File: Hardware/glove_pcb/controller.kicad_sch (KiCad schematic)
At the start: 10 parts, among them J6 ISCP, J7 Debug Serial, U2 MCP3008, U4 ATmega328PB-A

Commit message: Finish controller pin assignments
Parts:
- added C18, C20: 10uF, symbol Device:C
- added C19, C21: 0.1uF, symbol Device:C
- added J19: Bluetooth, symbol Connector_Generic:Conn_01x06
- added R7: 1k, symbol Device:R
- added R8: 2k, symbol Device:R
- added U6, U7: MCP3008, symbol Analog_ADC:MCP3008
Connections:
- net GND: now also C18.2, C19.2, C20.2, C21.2, J19.4 (Pin_4), R8.2, U6.14 (AGND), U6.9 (DGND), U7.14 (AGND), U7.9 (DGND)
- net MISO1: now also U6.12 (Dout), U7.12 (Dout)
- net MOSI1: now also U6.11 (Din), U7.11 (Din)
- net SCK1: now also U6.13 (CLK), U7.13 (CLK)
- net SS_ADC2: now also U6.10 (~{CS}/SHDN)
- net SS_ADC3: now also U7.10 (~{CS}/SHDN)
- net VCC_UC: now also C18.1, C19.1, C20.1, C21.1, U6.15 (Vref), U6.16 (Vdd), U7.15 (Vref), U7.16 (Vdd)
- net OC2B: now reaches U4.1 (PD3)
- net OC0A: now reaches U4.10 (PD6)
- net UC_MOTOR_PMODE: now reaches U4.11 (PD7)
- net UC_MOTOR_SLEEP: now reaches U4.12 (PB0)
- net OC1A: now reaches U4.13 (PB1)
- net OC1B: now reaches U4.14 (PB2)
- net MOTOR5_FAULT: now reaches U4.2 (PD4)
- net UC_MOTOR_PH2: now reaches U4.27 (PC4)
- net UC_MOTOR_PH3: now reaches U4.28 (PC5)
- net MOTOR3_FAULT: now reaches U4.3 (PE0)
- net RXD: now reaches U4.30 (PD0)
- net RXD: now also J19.3 (Pin_3)
- net TXD: now reaches U4.31 (PD1)
- net TXD: now also R7.1
- net UC_MOTOR_PH1: now reaches U4.32 (PD2)
- net MOTOR4_FAULT: now reaches U4.6 (PE1)
- net MOTOR1_FAULT: now reaches U4.7 (XTAL1/PB6)
- net MOTOR2_FAULT: now reaches U4.8 (XTAL2/PB7)
- net OC0B: now reaches U4.9 (PD5)
- new net: J19.2 (Pin_2), R7.2, R8.1
- new net VCC_BT: J19.5 (Pin_5)
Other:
- moved on the sheet: C12, C13, R6, U2

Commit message: Minor changes from meeting with dmitry
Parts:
- removed C8: 0.1uF, symbol Device:C
- removed J19: Bluetooth, symbol Connector_Generic:Conn_01x06
- removed R7: 1k, symbol Device:R
- removed R8: 2k, symbol Device:R
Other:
- moved on the sheet: C20, C21, R6, U7

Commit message: Yet more improvements to the schematic
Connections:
- net DBG_RX is gone; now on net MISO: J7.2 (Pin_2)
- net DBG_TX is gone; now on net MOSI: J7.3 (Pin_3)
- net GND: no longer J7.5 (Pin_5)
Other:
- moved on the sheet: C12, C13, C18, C19, C20, C21, U2, U6, U7

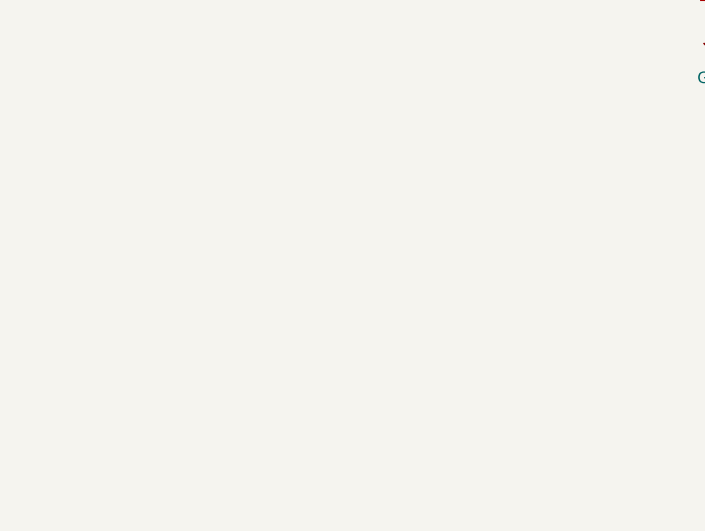
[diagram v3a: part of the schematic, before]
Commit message: Add logic level shifter to controller schematic
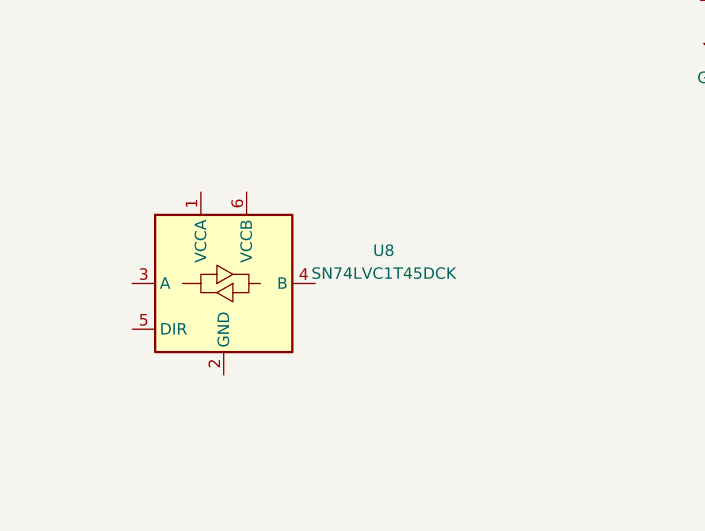
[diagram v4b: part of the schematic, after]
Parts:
- added U8: SN74LVC1T45DCK, Package_TO_SOT_SMD:SOT-363_SC-70-6, symbol Logic_LevelTranslator:SN74LVC1T45DCK
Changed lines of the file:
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@@
+    )
+  )
+  (symbol (lib_id "Logic_LevelTranslator:SN74LVC1T45DCK") (at 40.64 138.43 0) (unit 1)
+    (in_bom yes) (on_board yes) (dnp no) (fields_autoplaced)
+    (property "Reference" "U8" (at 58.42 134.7821 0)
+      (effects (font (size 1.27 1.27)))
+    )
+    (property "Value" "SN74LVC1T45DCK" (at 58.42 137.3221 0)
+      (effects (font (size 1.27 1.27)))
+    )
+    (property "Footprint" "Package_TO_SOT_SMD:SOT-363_SC-70-6" (at 40.64 149.86 0)
+      (effects (font (size 1.27 1.27)) hide)
+    )
+    (property "Datasheet" "http://www.ti.com/lit/ds/symlink/sn74lvc1t45.pdf" (at 17.78 154.94 0)
+      (effects (font (size 1.27 1.27)) hide)
+    )
+    (pin "1")
+    (pin "5")
+    (pin "4")
+    (pin "2")
+    (pin "6")
+    (pin "3")
+    (instances
+      (project "glove_pcb"
+        (path "/747ff5f3-d342-40b0-8e4e-75b3a3063e75/ecec443b-784e-4f7b-9f78-072e3afadba0"
+          (reference "U8") (unit 1)
+        )
+      )
     )
   )

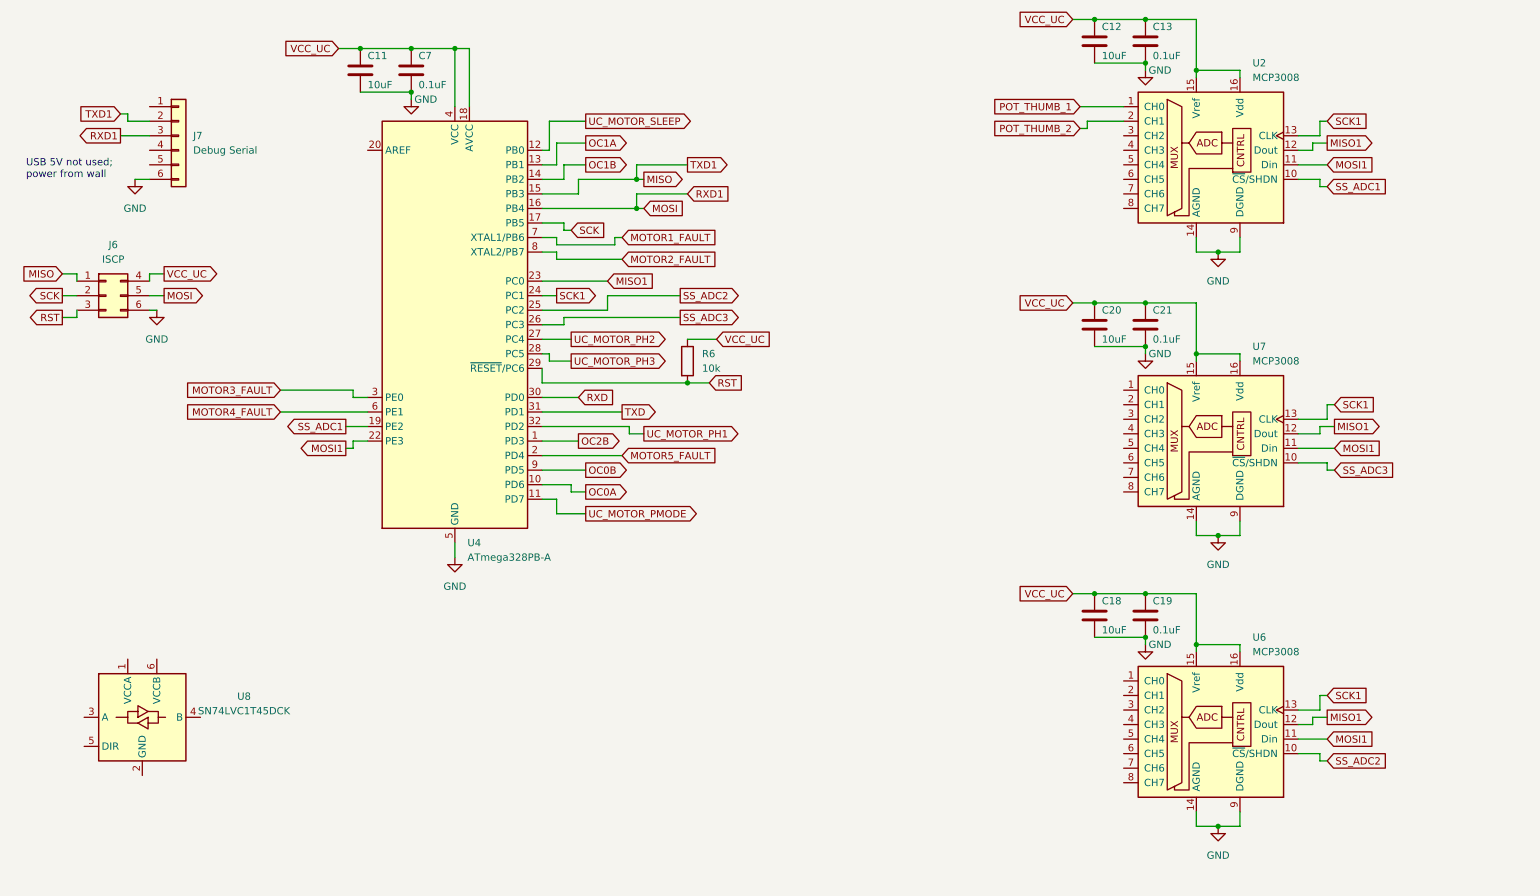
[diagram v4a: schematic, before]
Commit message: Finish schematic
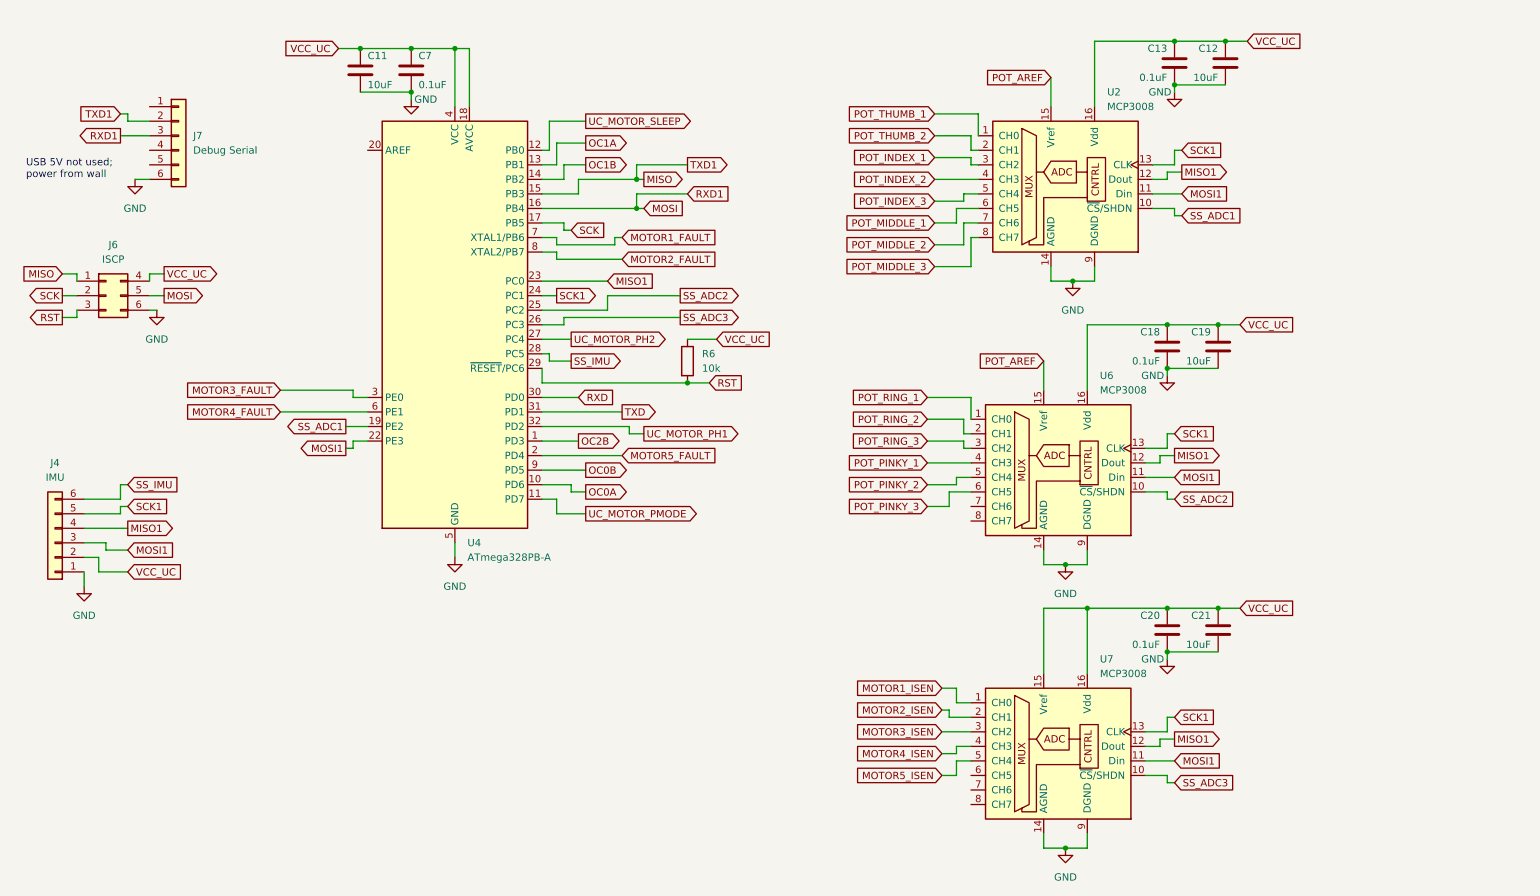
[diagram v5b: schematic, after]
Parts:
- removed U8: SN74LVC1T45DCK, Package_TO_SOT_SMD:SOT-363_SC-70-6, symbol Logic_LevelTranslator:SN74LVC1T45DCK
- added J4: IMU, symbol Connector_Generic:Conn_01x06
- C18, C20: value 10uF -> 0.1uF
- C19, C21: value 0.1uF -> 10uF
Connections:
- net GND: now also J4.1 (Pin_1)
- net MISO1: now also J4.4 (Pin_4)
- net MOSI1: now also J4.3 (Pin_3)
- net SCK1: now also J4.5 (Pin_5)
- net VCC_UC: now also J4.2 (Pin_2); no longer U2.15 (Vref), U6.15 (Vref)
- net POT_INDEX_1: now reaches U2.3 (CH2)
- net POT_INDEX_2: now reaches U2.4 (CH3)
- net POT_INDEX_3: now reaches U2.5 (CH4)
- net POT_MIDDLE_1: now reaches U2.6 (CH5)
- net POT_MIDDLE_2: now reaches U2.7 (CH6)
- net POT_MIDDLE_3: now reaches U2.8 (CH7)
- net MOTOR1_ISEN: now reaches U7.1 (CH0)
- net MOTOR2_ISEN: now reaches U7.2 (CH1)
- net MOTOR3_ISEN: now reaches U7.3 (CH2)
- net MOTOR4_ISEN: now reaches U7.4 (CH3)
- net MOTOR5_ISEN: now reaches U7.5 (CH4)
- net POT_RING_1: now reaches U6.1 (CH0)
- net POT_RING_2: now reaches U6.2 (CH1)
- net POT_RING_3: now reaches U6.3 (CH2)
- net POT_PINKY_1: now reaches U6.4 (CH3)
- net POT_PINKY_2: now reaches U6.5 (CH4)
- net POT_PINKY_3: now reaches U6.6 (CH5)
- net UC_MOTOR_PH3 renamed SS_IMU
- net SS_IMU: now also J4.6 (Pin_6)
- new net POT_AREF: U2.15 (Vref), U6.15 (Vref)
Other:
- moved on the sheet: C12, C13, U2

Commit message: Add titles to pages and reannotate
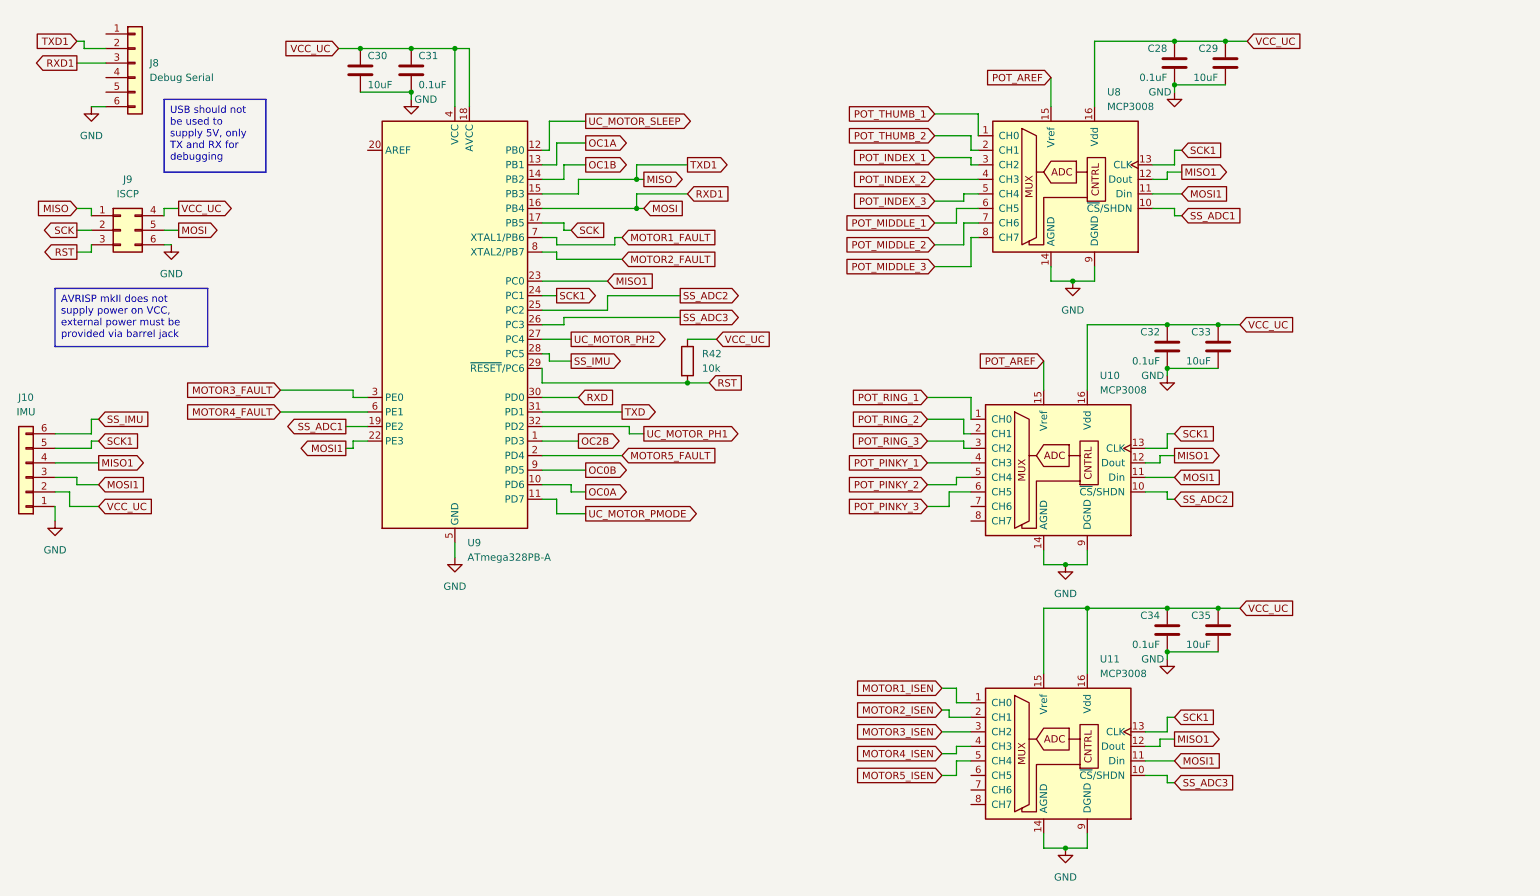
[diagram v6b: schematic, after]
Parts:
- renumbered C13 to C28, C12 to C29, C11 to C30, C7 to C31, C18 to C32, C19 to C33, C20 to C34, C21 to C35, J4 to J10, J7 to J8, J6 to J9, R6 to R42, U6 to U10, U7 to U11, U2 to U8, U4 to U9
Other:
- note removed: "USB 5V not used; power from wall"
- company: (none) -> COEN 490 Team 15
- title: (none) -> Microcontroller and Peripherals
- moved on the sheet: J10, J8, J9

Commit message: Finalize schematic for real this time
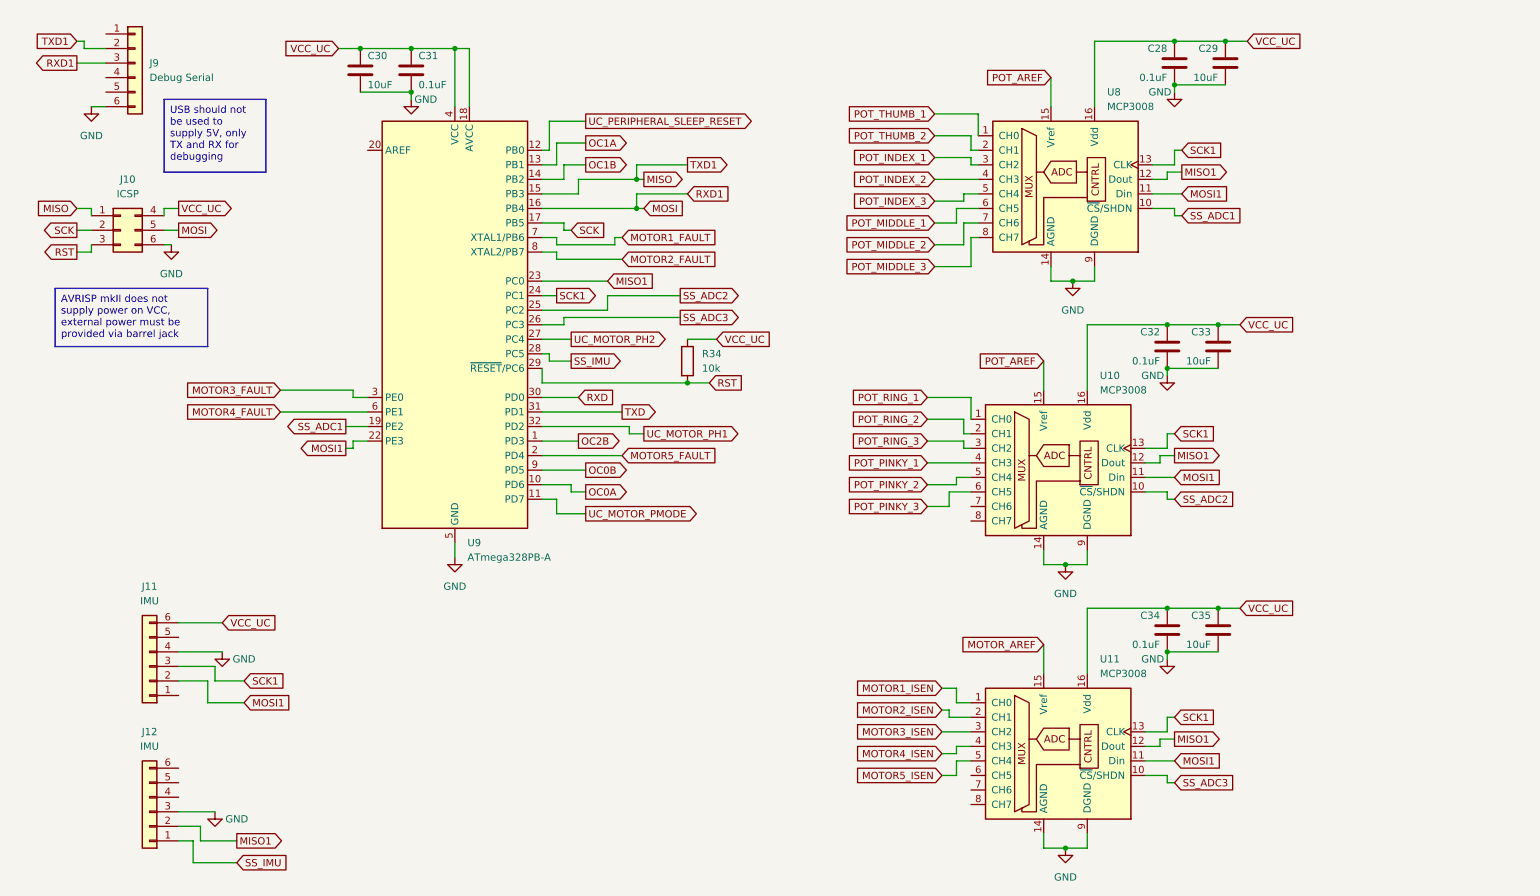
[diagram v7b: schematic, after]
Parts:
- removed J10: IMU, symbol Connector_Generic:Conn_01x06
- added J11, J12: IMU, symbol Connector_Generic:Conn_01x06
- J10: renamed from J9; value ISCP -> ICSP
- renumbered J8 to J9, R42 to R34
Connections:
- net GND: now also J11.4 (Pin_4), J12.3 (Pin_3)
- net MISO1: now also J12.2 (Pin_2)
- net MOSI1: now also J11.2 (Pin_2)
- net SCK1: now also J11.3 (Pin_3)
- net SS_IMU: now also J12.1 (Pin_1)
- net VCC_UC: now also J11.6 (Pin_6); no longer U11.15 (Vref)
- net UC_MOTOR_SLEEP renamed UC_PERIPHERAL_SLEEP_RESET
- new net MOTOR_AREF: U11.15 (Vref)
